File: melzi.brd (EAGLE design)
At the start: 208.3 x 49.5 mm, 121 parts, among them IC5 7805DT, IC6 ATMEGA1284P, IC7 4050D, IC8 FT232RL-BASICSSOP, M1 RFP30N06LE, M2 RFP30N06LE, M3 RFP30N06LE, Q1 16MHZ, U1 A4982, U2 A4982, U3 A4982, U4 A4982, X1 MICROSD, X2 MINI-USB-SHIELD-UX60-MB-5ST

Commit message: Thermistor resistors changed to 4K7.
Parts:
- R4, R5: value 10k -> 4k7
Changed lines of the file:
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@@
 <layer number="21" name="tPlace" color="7" fill="1" visible="yes" active="yes"/>
 <layer number="22" name="bPlace" color="7" fill="1" visible="no" active="yes"/>
-<layer number="23" name="tOrigins" color="15" fill="1" visible="no" active="yes"/>
+<layer number="23" name="tOrigins" color="15" fill="1" visible="yes" active="yes"/>
 <layer number="24" name="bOrigins" color="15" fill="1" visible="no" active="yes"/>
 <layer number="25" name="tNames" color="7" fill="1" visible="no" active="yes"/>
@@
 <element name="M3" library="SparkFun" package="DPAK" value="RFP30N06LE" x="146.05" y="30.48"/>
 <element name="R12" library="SparkFun" package="1206" value="10k" x="138.43" y="24.13" rot="R180"/>
-<element name="R4" library="SparkFun" package="1206" value="10k" x="189.23" y="33.02" rot="R90"/>
+<element name="R4" library="SparkFun" package="1206" value="4k7" x="189.23" y="33.02" rot="R90"/>
 <element name="C8" library="rcl" package="SMC_C" value="4.7 uF" x="185.42" y="31.75" rot="R270"/>
-<element name="R5" library="SparkFun" package="1206" value="10k" x="199.39" y="33.02" rot="R90"/>
+<element name="R5" library="SparkFun" package="1206" value="4k7" x="199.39" y="33.02" rot="R90"/>
 <element name="C9" library="rcl" package="SMC_C" value="4.7 uF" x="195.58" y="31.75" rot="R270"/>
 <element name="C28" library="rcl" package="UD-6,3X7,7_NICHICON" value="100 uF" x="107.95" y="30.48" smashed="yes" rot="R90">

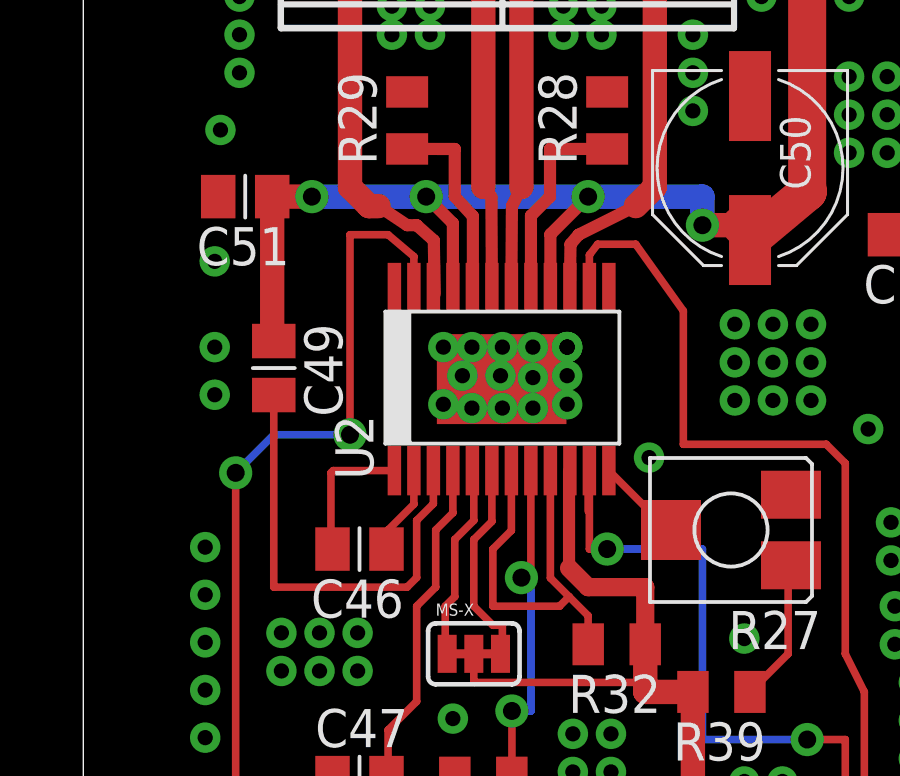
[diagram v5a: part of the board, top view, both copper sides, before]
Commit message: Gaps between ground plane and tracks upped to 10 thou.
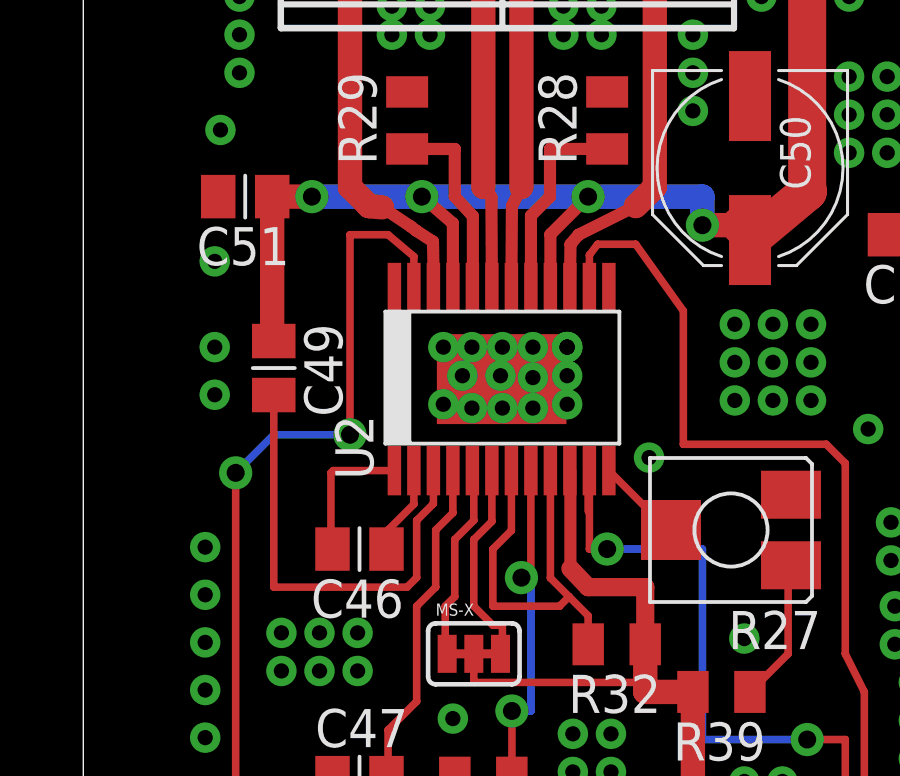
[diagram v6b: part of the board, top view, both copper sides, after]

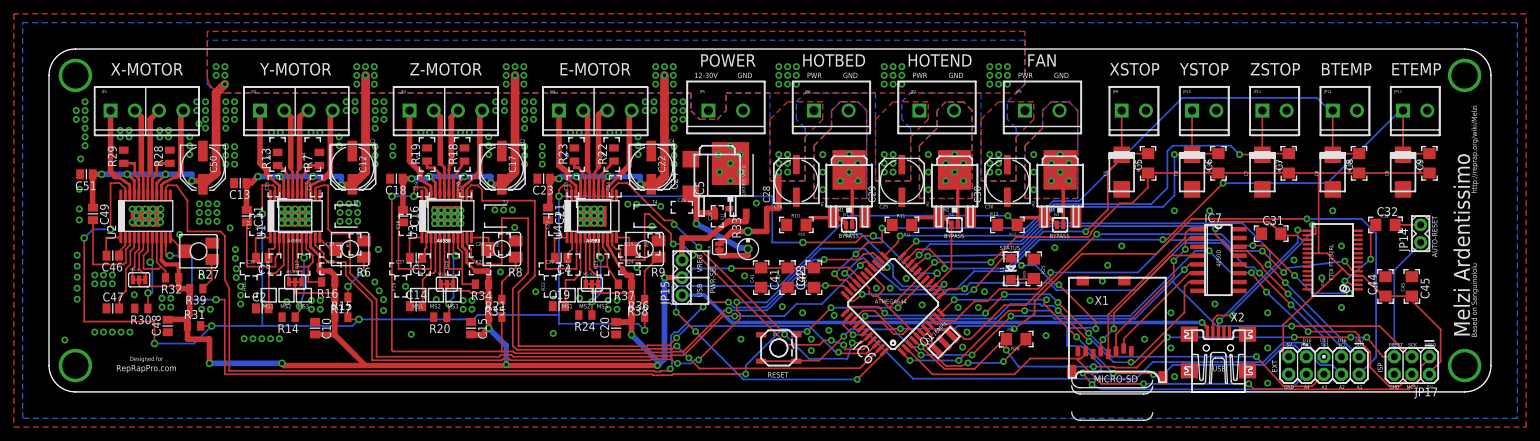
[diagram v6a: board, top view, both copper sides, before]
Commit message: Made motor current pots turn the right way.
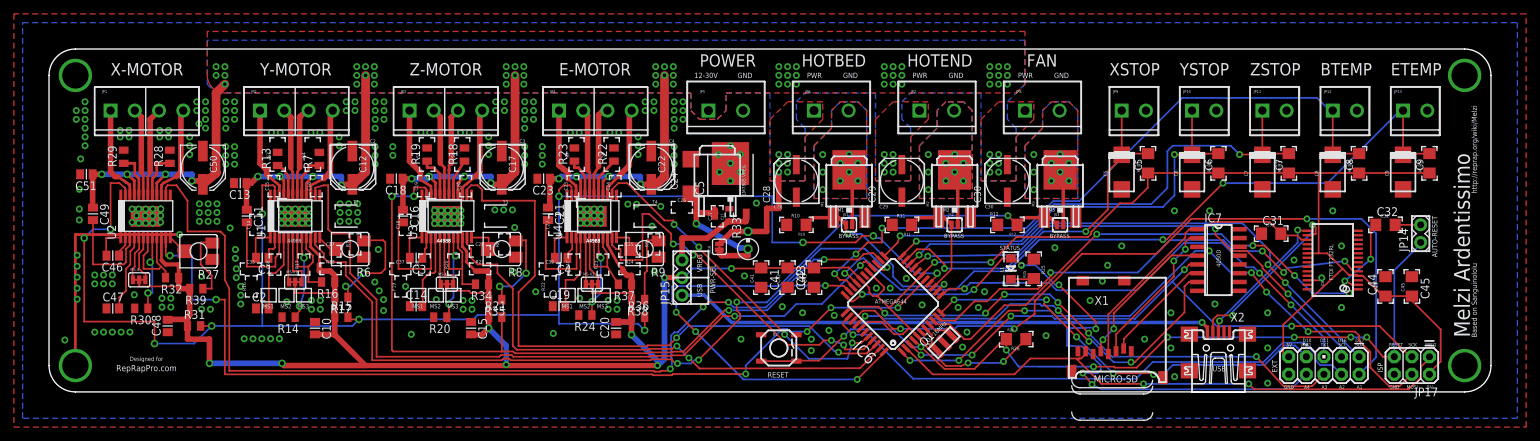
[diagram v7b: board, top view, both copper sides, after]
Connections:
- net GND: now also R27.1, R6.1, R8.1, R9.1; no longer R27.2, R6.2, R8.2, R9.2
- net N$46: now also R6.2; no longer R6.1
- net N$59: now also R8.2; no longer R8.1
- net N$69: now also R27.2; no longer R27.1
- net N$74: now also R9.2; no longer R9.1
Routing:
- net GND: track 0.00 -> 36.4 mm
- net Z-STEP: track 93.9 -> 76.1 mm
- net N$46: track 6.96 -> 15.5 mm
- net N$59: track 6.96 -> 12.9 mm, vias 0 -> 2
- net N$69: track 4.79 -> 10.3 mm
- net N$74: track 6.96 -> 10.4 mm
- net N$7: track 3.60 -> 4.33 mm
